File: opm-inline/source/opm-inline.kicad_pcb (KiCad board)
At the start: 4 copper layers, 58 x 40 mm, 71 parts, among them IC1 TMC6200-TA, J1 Info, J2 VCC_IO, J3 PWMx6, J4 Fan, J6 Current Sensing, Q1 HYG025N06LS1C2, Q2 HYG025N06LS1C2, Q3 HYG025N06LS1C2, Q4 HYG025N06LS1C2, Q5 HYG025N06LS1C2, Q6 HYG025N06LS1C2, U2 TerminalBlock_2_P5.08mm, U3 TerminalBlock_3_P5.08mm

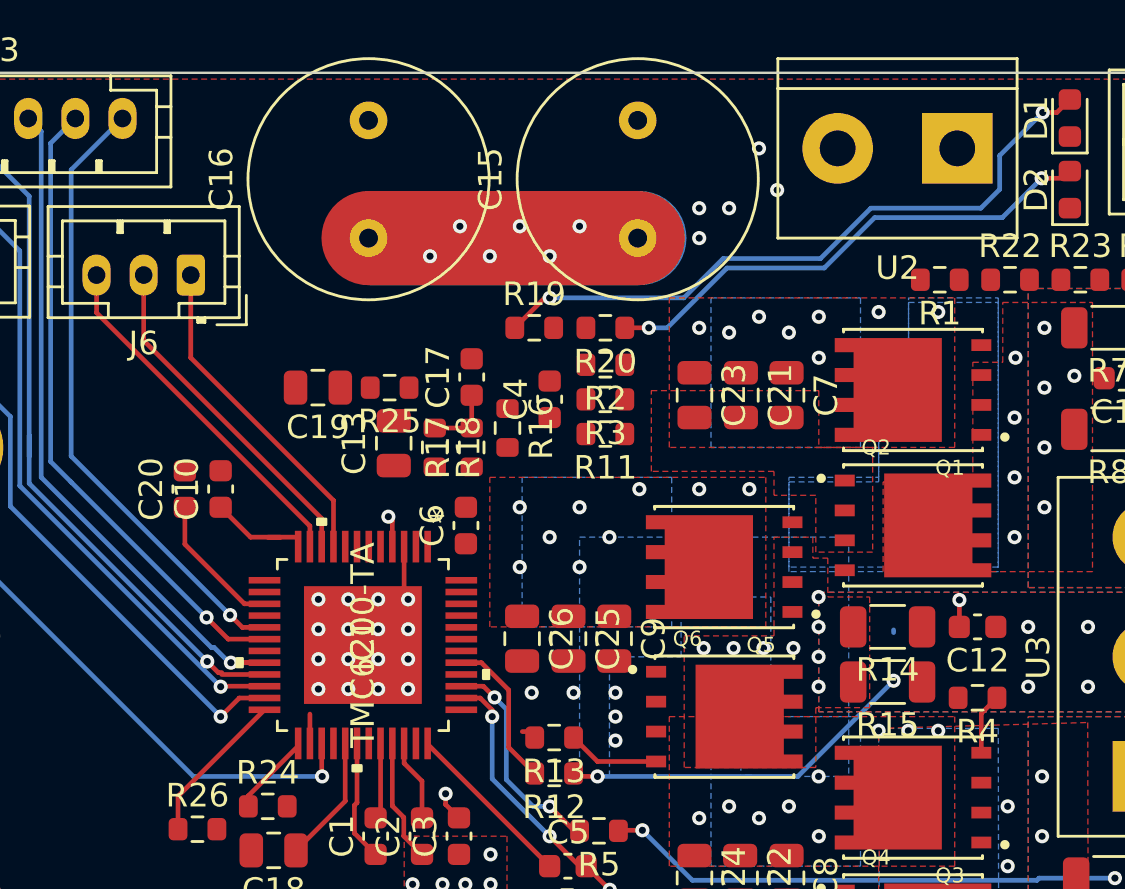
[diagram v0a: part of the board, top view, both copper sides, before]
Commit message: route tracks
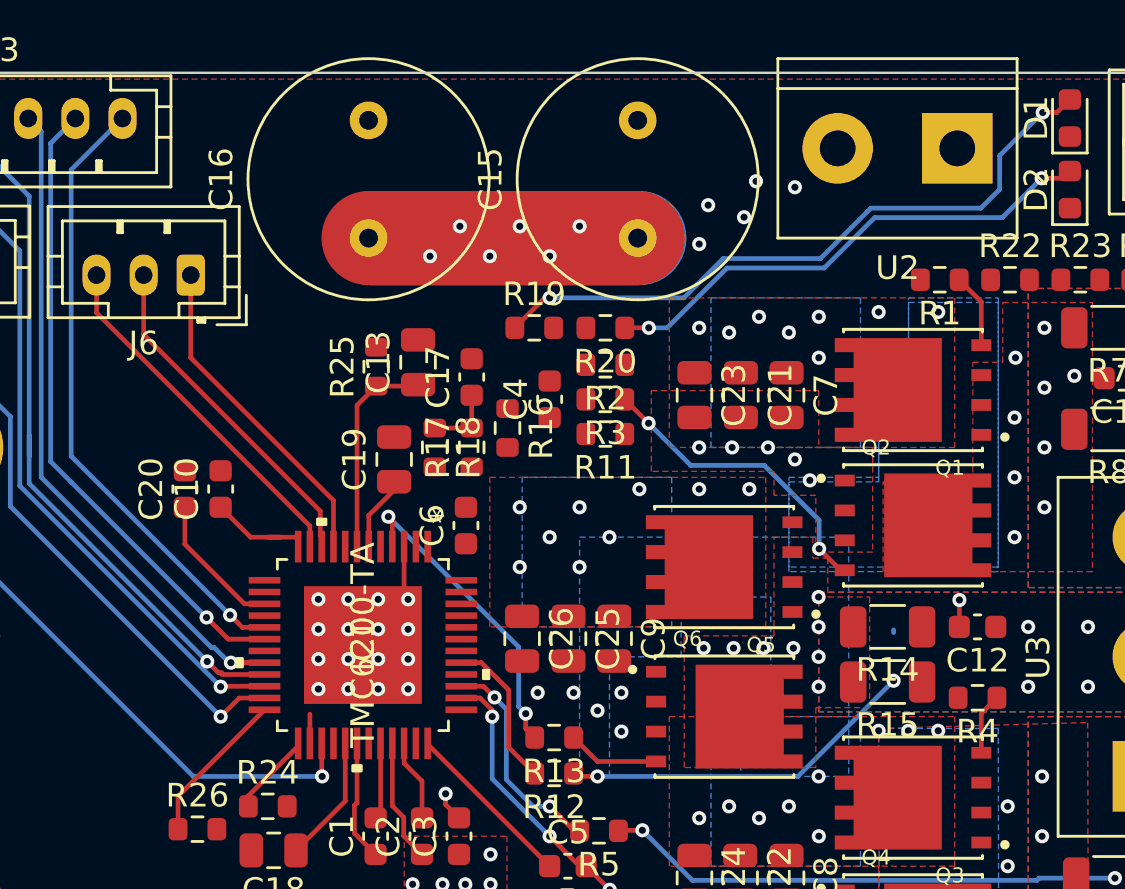
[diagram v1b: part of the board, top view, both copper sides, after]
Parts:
- moved C19 4.45 mm to (153.4, 83.1), turned to 90 degrees
- moved C13 3.59 mm to (154.4, 78.9)
- moved R25 1.06 mm to (152.7, 79.1), turned to 90 degrees
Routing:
- net Net-(Q2-Pad4): track 0.00 -> 13.2 mm, vias 0 -> 2
- net Net-(IC1-Pad4): track 1.74 -> 13.3 mm, vias 1 -> 2
- net /5Vout: track 0.00 -> 8.96 mm
- net /12Vout: track 0.00 -> 3.20 mm
- net Net-(Q1-Pad4): track 0.00 -> 3.16 mm
- net GND: vias 25 -> 30

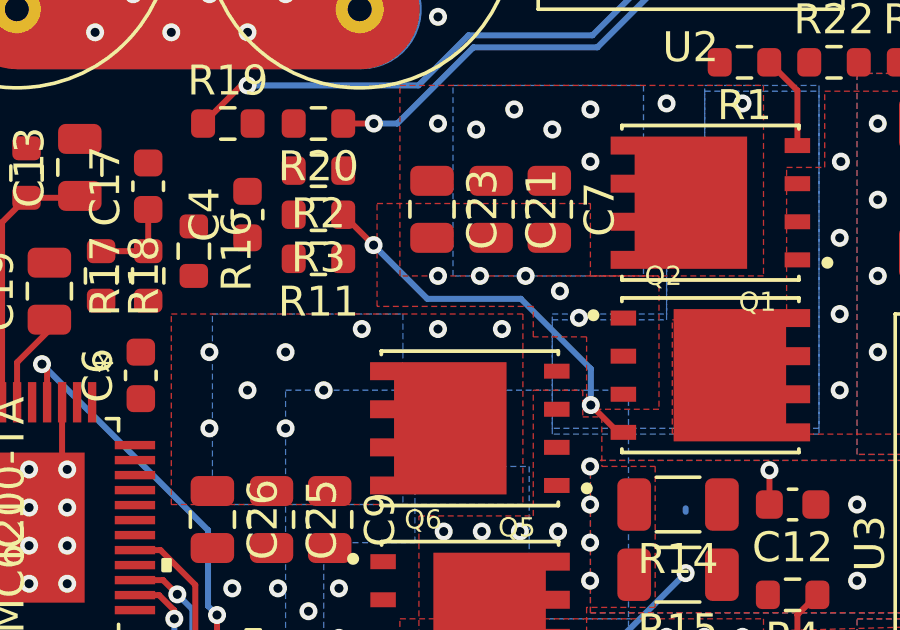
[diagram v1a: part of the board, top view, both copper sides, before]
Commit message: route tracks
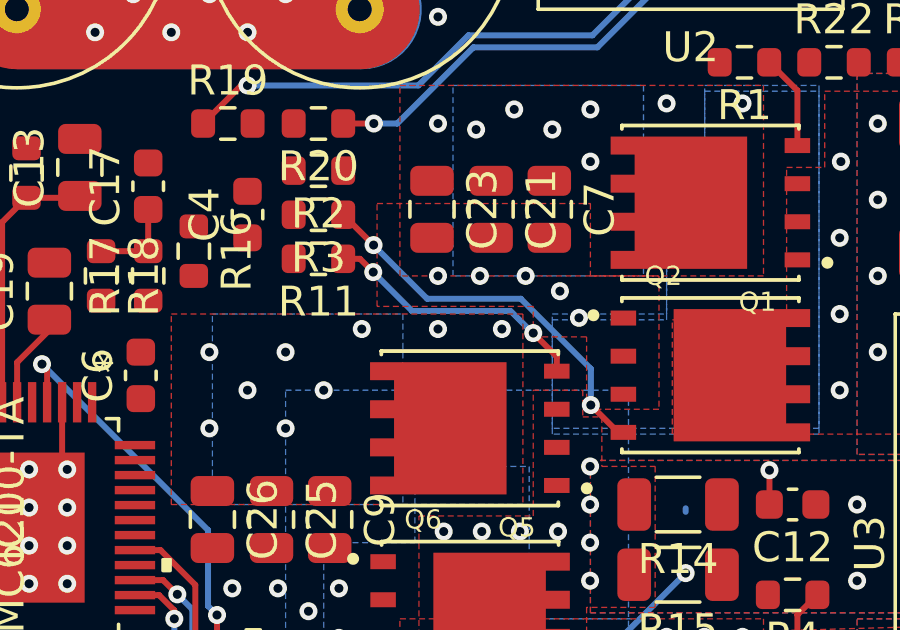
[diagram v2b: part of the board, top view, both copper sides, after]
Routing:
- net Net-(Q5-Pad4): track 0.00 -> 8.96 mm, vias 0 -> 2
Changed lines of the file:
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@@
     (thickness 1.6)
     (drawings 4)
-    (tracks 339)
+    (tracks 349)
     (zones 0)
     (modules 71)
@@
   (gr_line (start 187.96 66.64) (end 187.96 106.63) (layer Edge.Cuts) (width 0.1))
   (gr_line (start 187.96 106.63) (end 130.01 106.63) (layer Edge.Cuts) (width 0.1))
+  (via (at 169.545 84.455) (size 0.6) (drill 0.3) (layers F.Cu B.Cu) (net 45))
+  (via (at 164.211 82.423) (size 0.6) (drill 0.3) (layers F.Cu B.Cu) (net 45))
   (via (at 159.004 93.853) (size 0.6) (drill 0.3) (layers F.Cu B.Cu) (net 21))
   (via (at 162.052 96.52) (size 0.6) (drill 0.3) (layers F.Cu B.Cu) (net 14))
@@
   (segment (start 164.915 105.175) (end 171.431 105.175) (width 0.2) (layer B.Cu) (net 44))
   (segment (start 162.458 102.718) (end 164.915 105.175) (width 0.2) (layer B.Cu) (net 44))
+  (segment (start 163.768 81.98) (end 164.211 82.423) (width 0.2) (layer F.Cu) (net 45))
+  (segment (start 163.21 81.98) (end 163.768 81.98) (width 0.2) (layer F.Cu) (net 45))
+  (segment (start 170.33 85.24) (end 169.545 84.455) (width 0.2) (layer F.Cu) (net 45))
+  (segment (start 170.33 85.725) (end 170.33 85.24) (width 0.2) (layer F.Cu) (net 45))
+  (segment (start 165.507999 83.719999) (end 164.211 82.423) (width 0.2) (layer B.Cu) (net 45))
+  (segment (start 168.788001 83.719999) (end 165.507999 83.719999) (width 0.2) (layer B.Cu) (net 45))
+  (segment (start 169.523002 84.455) (end 168.788001 83.719999) (width 0.2) (layer B.Cu) (net 45))
+  (segment (start 169.545 84.455) (end 169.523002 84.455) (width 0.2) (layer B.Cu) (net 45))
   (segment (start 162.051 95.885) (end 161.035 94.869) (width 0.2) (layer F.Cu) (net 46))
   (segment (start 164.54 95.885) (end 162.051 95.885) (width 0.2) (layer F.Cu) (net 46))

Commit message: use pins
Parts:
- moved C6 13.6 mm to (163.6, 97.4), turned to 180 degrees
- moved HS1 13.4 mm to (238.3, 100.6)
- moved C17 8.79 mm to (148.1, 77.9), turned to 270 degrees
- moved R17 8.50 mm to (149.6, 77.9)
- moved R16 7.39 mm to (150.9, 81.0), turned to 90 degrees
- moved R18 6.10 mm to (151.1, 78.0), turned to 90 degrees
- moved C4 4.33 mm to (156.0, 82.0), turned to 180 degrees
- moved C10 0.64 mm to (145.5, 84.7)
- moved C20 0.64 mm to (144.0, 84.7)
- moved R22 0.07 mm to (179.6, 75.4)
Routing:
- net /TEMP_PCB: track 2.96 -> 36.4 mm, vias 0 -> 1
- net Net-(IC1-Pad48): track 0.00 -> 25.6 mm, vias 0 -> 2
- net Net-(C6-Pad1): track 0.00 -> 19.3 mm, vias 8 -> 10
- net Net-(C6-Pad2): track 0.00 -> 11.6 mm, vias 0 -> 2
- net Net-(C4-Pad1): track 0.00 -> 7.79 mm, vias 8 -> 9
- net Net-(C4-Pad2): track 0.00 -> 4.87 mm
- net Net-(R16-Pad2): track 0.00 -> 1.95 mm
- net Net-(IC1-Pad5): track 0.00 -> 1.42 mm, vias 0 -> 1
- removed copper zone on B.Cu, net Net-(C5-Pad2)
- removed copper zone on B.Cu, net Net-(C6-Pad1)

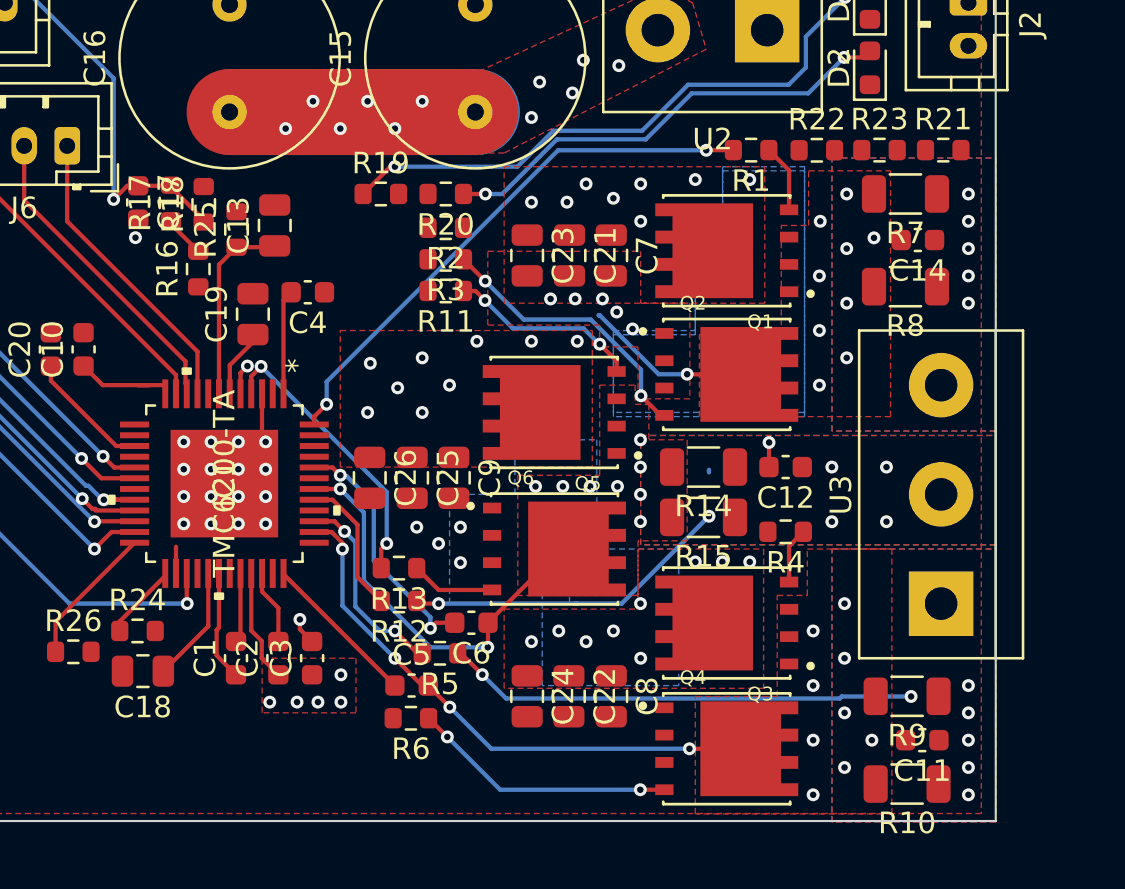
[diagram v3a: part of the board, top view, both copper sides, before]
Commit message: route tracks
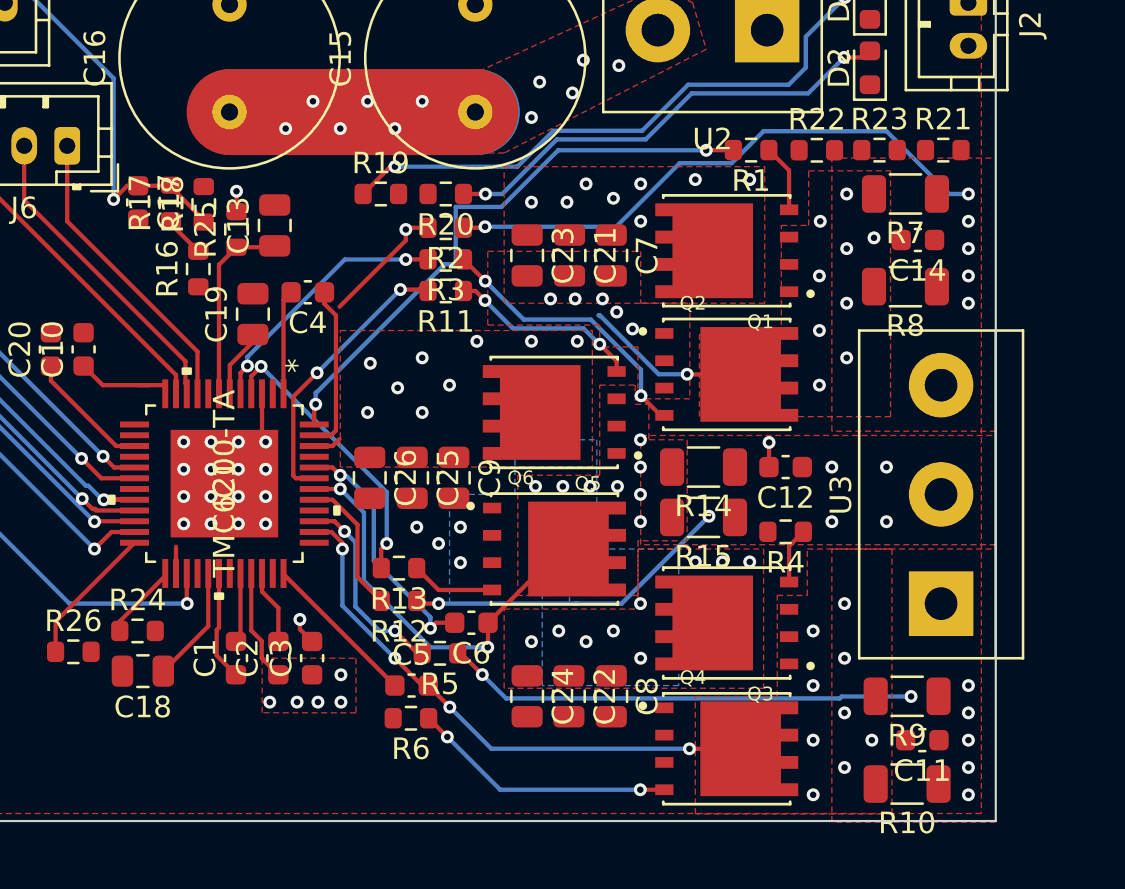
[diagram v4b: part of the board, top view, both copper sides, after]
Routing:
- net /U: track 0.00 -> 26.6 mm, vias 5 -> 6
- net Net-(IC1-Pad43): track 0.00 -> 13.1 mm, vias 0 -> 2
- net Net-(IC1-Pad5): track 1.42 -> 12.1 mm, vias 1 -> 2
- net Net-(C4-Pad1): track 7.79 -> 16.0 mm
- net Net-(IC1-Pad46): track 0.00 -> 7.25 mm, vias 0 -> 1
- net Net-(IC1-Pad48): track 25.6 -> 27.2 mm
- net /+VM: track 70.3 -> 71.2 mm, vias 42 -> 43
- net GND: vias 30 -> 29
- removed copper zone on B.Cu, net /U
- removed copper zone on B.Cu, net /V
- removed copper zone on B.Cu, net /W
- removed copper zone on B.Cu, net Net-(C4-Pad1)
- removed copper zone on B.Cu, net Net-(R2-Pad1)

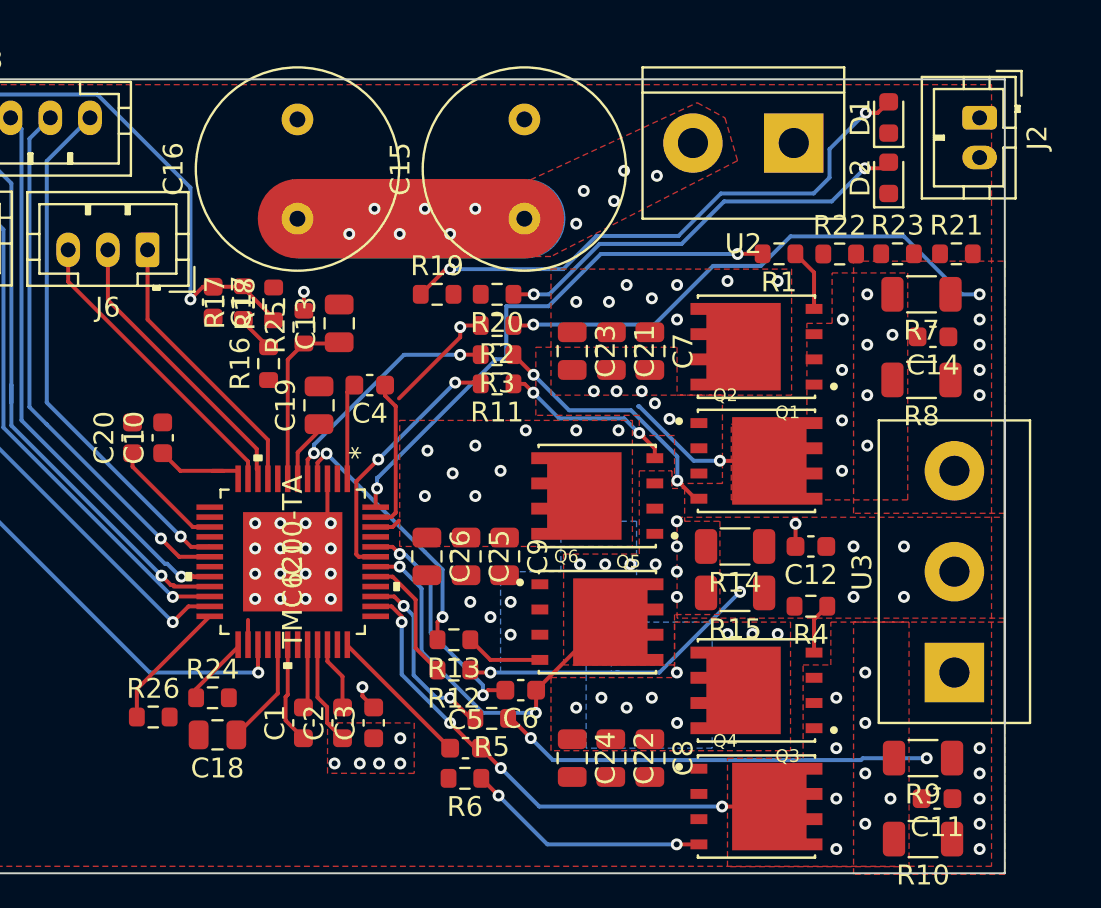
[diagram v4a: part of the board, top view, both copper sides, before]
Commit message: route tracks
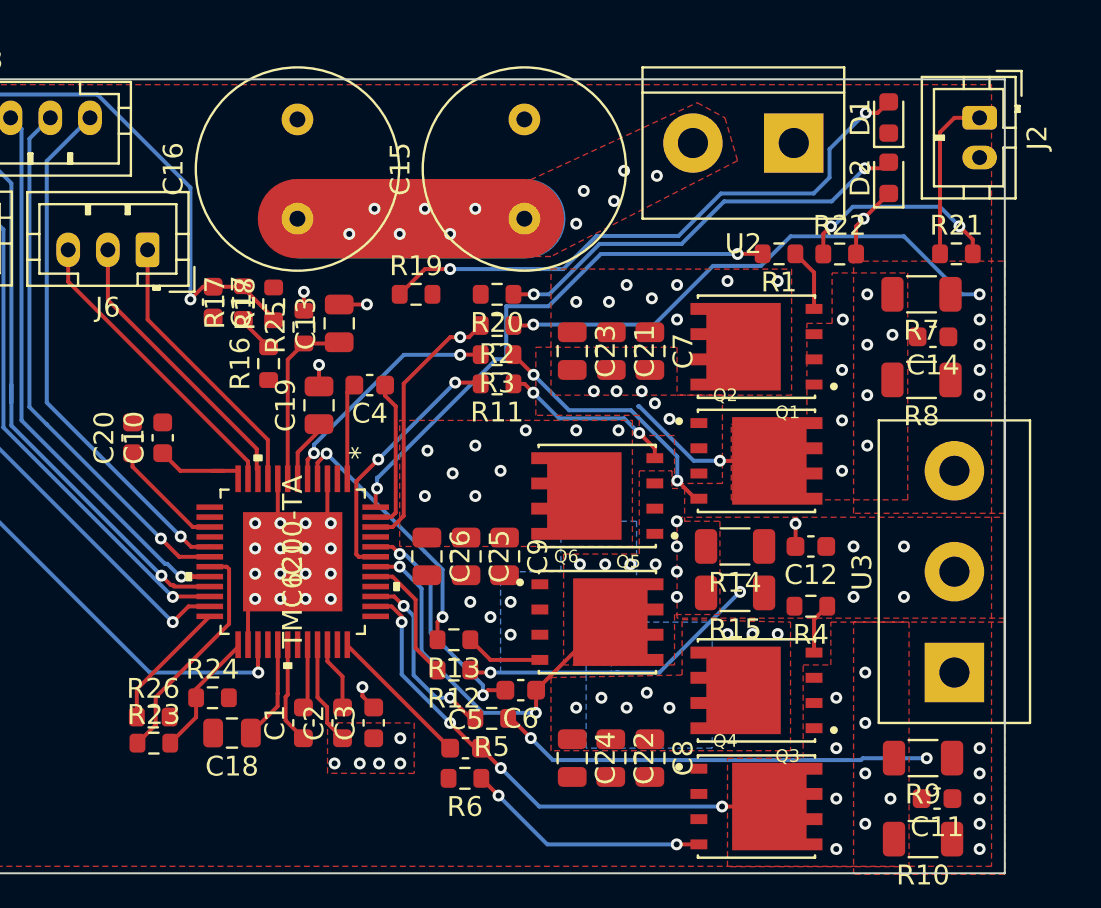
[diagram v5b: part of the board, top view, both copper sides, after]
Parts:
- moved R23 44.8 mm to (145.1, 100.1)
- moved R19 1.06 mm to (158.3, 77.5)
- moved C18 0.74 mm to (149.0, 99.6)
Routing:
- net /+VCC_IO: track 5.82 -> 25.9 mm
- net GND: track 8.55 -> 23.1 mm, vias 29 -> 32
- net /Connectors/VOFS: track 0.00 -> 10.5 mm, vias 0 -> 2
- net Net-(IC1-Pad46): track 7.25 -> 13.4 mm
- net /SPE: track 3.55 -> 6.37 mm
- net Net-(D1-Pad2): track 28.4 -> 29.7 mm
- net /+VM: vias 43 -> 42
